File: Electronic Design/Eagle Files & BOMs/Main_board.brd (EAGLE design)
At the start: 99.9 x 68 mm, 36 parts, among them IC1 ACS712ELC-5A, IC2 ATMEGA328-PU, Q1 IRF9540, Q2 IRF9540, X1 16MHz

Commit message: adding header for additional DIO pins
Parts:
- added JP1: (no value), pinhead:1X05
- moved R5 8.54 mm to (79.1, 64.6), turned to 180 degrees
- moved S2 4.76 mm to (91.0, 63.8), turned to 180 degrees
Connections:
- new net N$20: IC2.14, JP1.5
- new net N$21: IC2.13, JP1.4
- new net N$22: IC2.12, JP1.3
- new net N$25: IC2.11, JP1.2
- net +5V: now also S2.2; no longer S2.1
- net GND: now also JP1.1
- net N$8: now also S2.4; no longer S2.3
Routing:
- net N$22: track 0.00 -> 14.9 mm
- net N$20: track 0.00 -> 14.9 mm
- net N$21: track 0.00 -> 14.9 mm
- net N$25: track 0.00 -> 14.8 mm
- net +5V: track 124.9 -> 111.1 mm
- net N$8: track 35.0 -> 34.0 mm
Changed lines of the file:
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@@
 <attribute name="VALUE" x="69.206034375" y="0.859565625" size="1.27" layer="27"/>
 </element>
-<element name="S2" library="switch-omron" package="B3F-10XX" value="" x="93.486315625" y="59.761790625" rot="R270">
-<attribute name="MPN" value="B3F-1000" x="93.486315625" y="59.761790625" size="1.778" layer="27" rot="R270" display="off"/>
-<attribute name="OC_FARNELL" value="176432" x="93.486315625" y="59.761790625" size="1.778" layer="27" rot="R270" display="off"/>
-<attribute name="OC_NEWARK" value="36M3542" x="93.486315625" y="59.761790625" size="1.778" layer="27" rot="R270" display="off"/>
-<attribute name="MF" value="" x="93.486315625" y="59.761790625" size="1.778" layer="27" rot="R270" display="off"/>
+<element name="S2" library="switch-omron" package="B3F-10XX" value="" x="91.021790625" y="63.833684375" rot="R180">
+<attribute name="MPN" value="B3F-1000" x="91.021790625" y="63.833684375" size="1.778" layer="27" rot="R180" display="off"/>
+<attribute name="OC_FARNELL" value="176432" x="91.021790625" y="63.833684375" size="1.778" layer="27" rot="R180" display="off"/>
+<attribute name="OC_NEWARK" value="36M3542" x="91.021790625" y="63.833684375" size="1.778" layer="27" rot="R180" display="off"/>
+<attribute name="MF" value="" x="91.021790625" y="63.833684375" size="1.778" layer="27" rot="R180" display="off"/>
 </element>
-<element name="R5" library="resistor" package="R1206" value="10k" x="87.245540625" y="62.122259375" rot="R90"/>
+<element name="R5" library="resistor" package="R1206" value="10k" x="79.077740625" y="64.605540625" rot="R180"/>
 <element name="POT1" library="resistor" package="RTRIM3296W" value="500k" x="63.175203125" y="54.911571875"/>
 <element name="D1" library="diode" package="DO35Z10" value="5.1V" x="70.7402" y="23.7643125" rot="R270"/>
@@
 </element>
 <element name="R6" library="varistor" package="S14K17" value="S14K75" x="15.67" y="51.73" rot="R270"/>
+<element name="JP1" library="pinhead" package="1X05" value="" x="97.05" y="53.75" smashed="yes" rot="R90">
+<attribute name="NAME" x="94.4312" y="54.2438" size="1.27" layer="25" ratio="10" rot="R90"/>
+<attribute name="VALUE" x="100.225" y="48.67" size="1.27" layer="27" rot="R90"/>
+</element>
 </elements>
 <signals>
@@
 <via x="89.61569375" y="42.3402" extent="1-16" drill="0.6" shape="square"/>
 <via x="89.41569375" y="39.5402" extent="1-16" drill="0.6" shape="square"/>
-<via x="94.41569375" y="49.1402" extent="1-16" drill="0.6" shape="square"/>
-<via x="85.81569375" y="54.5402" extent="1-16" drill="0.6" shape="square"/>
-<via x="87.81569375" y="54.1402" extent="1-16" drill="0.6" shape="square"/>
-<via x="92.61569375" y="54.5402" extent="1-16" drill="0.6" shape="square"/>
+<via x="93.97569375" y="47.0202" extent="1-16" drill="0.6" shape="square"/>
+<via x="59.33569375" y="57.8102" extent="1-16" drill="0.6" shape="square"/>
+<via x="49.50569375" y="60.0602" extent="1-16" drill="0.6" shape="square"/>
+<via x="96.14569375" y="31.6502" extent="1-16" drill="0.6" shape="square"/>
 <via x="87.81569375" y="44.3402" extent="1-16" drill="0.6" shape="square"/>
-<via x="94.324609375" y="52.94186875" extent="1-16" drill="0.6" shape="square"/>
+<via x="94.324609375" y="49.50186875" extent="1-16" drill="0.6" shape="square"/>
 <via x="92.8973" y="41.040346875" extent="1-16" drill="0.6" shape="square"/>
 <via x="75.41569375" y="63.5402" extent="1-16" drill="0.6" shape="square"/>
@@
 <vertex x="100.32" y="68.47"/>
 </polygon>
+<contactref element="JP1" pad="1"/>
 </signal>
 <signal name="M1S">
@@
 <wire x1="76.64795625" y1="47.329528125" x2="75.3559375" y2="47.329528125" width="0.6096" layer="1"/>
 <wire x1="75.3559375" y1="47.329528125" x2="75.1825375" y2="47.502928125" width="0.6096" layer="1"/>
-<contactref element="S2" pad="1"/>
 <wire x1="82.8025375" y1="42.422928125" x2="86.31648125" y2="42.422928125" width="0.6096" layer="1"/>
 <wire x1="86.31648125" y1="42.422928125" x2="86.71648125" y2="42.16599375" width="0.6096" layer="1"/>
@@
 <wire x1="75.1825375" y1="44.962928125" x2="69.234984375" y2="44.962928125" width="0.6096" layer="1"/>
 <wire x1="69.234984375" y1="44.962928125" x2="68.5950375" y2="45.00298125" width="0.6096" layer="1"/>
-<wire x1="95.746915625" y1="63.012990625" x2="95.746915625" y2="64.233084375" width="0.6096" layer="16"/>
-<wire x1="95.746915625" y1="64.233084375" x2="94.42" y2="65.56" width="0.6096" layer="16"/>
-<wire x1="94.42" y1="65.56" x2="79.22" y2="65.56" width="0.6096" layer="16"/>
-<wire x1="79.22" y1="65.56" x2="78.22" y2="64.56" width="0.6096" layer="16"/>
-<wire x1="78.22" y1="64.56" x2="78.22" y2="49.129528125" width="0.6096" layer="16"/>
-<wire x1="78.22" y1="49.129528125" x2="76.42" y2="47.329528125" width="0.6096" layer="16"/>
-<wire x1="76.42" y1="47.329528125" x2="75.3559375" y2="47.329528125" width="0.6096" layer="16"/>
-<wire x1="75.3559375" y1="47.329528125" x2="75.1825375" y2="47.502928125" width="0.6096" layer="16"/>
 <wire x1="68.5950375" y1="45.00298125" x2="67.23298125" y2="45.00298125" width="0.6096" layer="1"/>
 <wire x1="67.23298125" y1="45.00298125" x2="66.04" y2="43.81" width="0.6096" layer="1"/>
@@
 <wire x1="85.68" y1="13.68" x2="87.735384375" y2="13.68" width="0.6096" layer="1"/>
 <wire x1="87.735384375" y1="13.68" x2="87.81119375" y2="13.604190625" width="0.6096" layer="1"/>
+<contactref element="S2" pad="2"/>
+<wire x1="87.770590625" y1="61.573084375" x2="79.543084375" y2="61.573084375" width="0.6096" layer="16"/>
+<wire x1="79.543084375" y1="61.573084375" x2="78.61" y2="60.64" width="0.6096" layer="16"/>
+<wire x1="78.61" y1="60.64" x2="78.61" y2="48.94" width="0.6096" layer="16"/>
+<wire x1="78.61" y1="48.94" x2="77.28" y2="47.61" width="0.6096" layer="16"/>
+<wire x1="77.28" y1="47.61" x2="75.289609375" y2="47.61" width="0.6096" layer="16"/>
+<wire x1="75.289609375" y1="47.61" x2="75.1825375" y2="47.502928125" width="0.6096" layer="16"/>
 </signal>
 <signal name="N$15">
@@
 <signal name="N$8">
 <contactref element="IC2" pad="19"/>
-<contactref element="S2" pad="3"/>
 <contactref element="R5" pad="2"/>
 <contactref element="LED_CONTROL_OUT" pad="5"/>
-<wire x1="75.1825375" y1="50.042928125" x2="77.302928125" y2="50.042928125" width="0.6096" layer="1"/>
-<wire x1="77.302928125" y1="50.042928125" x2="78.82" y2="51.56" width="0.6096" layer="1"/>
-<wire x1="78.82" y1="51.56" x2="78.82" y2="62.76" width="0.6096" layer="1"/>
-<wire x1="78.82" y1="62.76" x2="79.62" y2="63.56" width="0.6096" layer="1"/>
-<wire x1="79.62" y1="63.56" x2="84.0298" y2="63.56" width="0.6096" layer="1"/>
-<wire x1="84.0298" y1="63.56" x2="87.245540625" y2="63.544259375" width="0.6096" layer="1"/>
-<wire x1="87.245540625" y1="63.544259375" x2="90.756984375" y2="63.544259375" width="0.6096" layer="1"/>
-<wire x1="90.756984375" y1="63.544259375" x2="91.225715625" y2="63.012990625" width="0.6096" layer="1"/>
 <wire x1="75.1825375" y1="50.042928125" x2="68.635090625" y2="50.042928125" width="0.6096" layer="1"/>
 <wire x1="68.635090625" y1="50.042928125" x2="68.5950375" y2="50.08298125" width="0.6096" layer="1"/>
+<contactref element="S2" pad="4"/>
+<wire x1="87.770590625" y1="66.094284375" x2="79.144484375" y2="66.094284375" width="0.6096" layer="1"/>
+<wire x1="79.144484375" y1="66.094284375" x2="77.655740625" y2="64.605540625" width="0.6096" layer="1"/>
+<wire x1="77.655740625" y1="64.605540625" x2="77.655740625" y2="50.705740625" width="0.6096" layer="1"/>
+<wire x1="77.655740625" y1="50.705740625" x2="76.92" y2="49.97" width="0.6096" layer="1"/>
+<wire x1="76.92" y1="49.97" x2="75.255465625" y2="49.97" width="0.6096" layer="1"/>
+<wire x1="75.255465625" y1="49.97" x2="75.1825375" y2="50.042928125" width="0.6096" layer="1"/>
 </signal>
 <signal name="N$4">
@@
 <wire x1="68.635090625" y1="39.882928125" x2="68.5950375" y2="39.92298125" width="0.6096" layer="1"/>
 </signal>
+<signal name="N$20">
+<contactref element="IC2" pad="14"/>
+<contactref element="JP1" pad="5"/>
+<wire x1="82.8025375" y1="60.202928125" x2="84.897071875" y2="60.202928125" width="0.6096" layer="1"/>
+<wire x1="84.897071875" y1="60.202928125" x2="86.35" y2="58.75" width="0.6096" layer="1"/>
+<wire x1="86.35" y1="58.75" x2="96.97" y2="58.75" width="0.6096" layer="1"/>
+<wire x1="96.97" y1="58.75" x2="97.05" y2="58.83" width="0.6096" layer="1"/>
+</signal>
+<signal name="N$21">
+<contactref element="IC2" pad="13"/>
+<contactref element="JP1" pad="4"/>
+<wire x1="82.8025375" y1="57.662928125" x2="93.187071875" y2="57.662928125" width="0.6096" layer="1"/>
+<wire x1="93.187071875" y1="57.662928125" x2="94.62" y2="56.23" width="0.6096" layer="1"/>
+<wire x1="94.62" y1="56.23" x2="96.99" y2="56.23" width="0.6096" layer="1"/>
+<wire x1="96.99" y1="56.23" x2="97.05" y2="56.29" width="0.6096" layer="1"/>
+</signal>
+<signal name="N$22">
+<contactref element="IC2" pad="12"/>
+<contactref element="JP1" pad="3"/>
+<wire x1="82.8025375" y1="55.122928125" x2="93.647071875" y2="55.122928125" width="0.6096" layer="1"/>
+<wire x1="93.647071875" y1="55.122928125" x2="95.11" y2="53.66" width="0.6096" layer="1"/>
+<wire x1="95.11" y1="53.66" x2="96.96" y2="53.66" width="0.6096" layer="1"/>
+<wire x1="96.96" y1="53.66" x2="97.05" y2="53.75" width="0.6096" layer="1"/>
+</signal>
+<signal name="N$25">
+<contactref element="IC2" pad="11"/>
+<contactref element="JP1" pad="2"/>
+<wire x1="82.8025375" y1="52.582928125" x2="93.577071875" y2="52.582928125" width="0.6096" layer="16"/>
+<wire x1="93.577071875" y1="52.582928125" x2="94.98" y2="51.18" width="0.6096" layer="16"/>
+<wire x1="94.98" y1="51.18" x2="97.02" y2="51.18" width="0.6096" layer="16"/>
+<wire x1="97.02" y1="51.18" x2="97.05" y2="51.21" width="0.6096" layer="16"/>
+</signal>
 </signals>

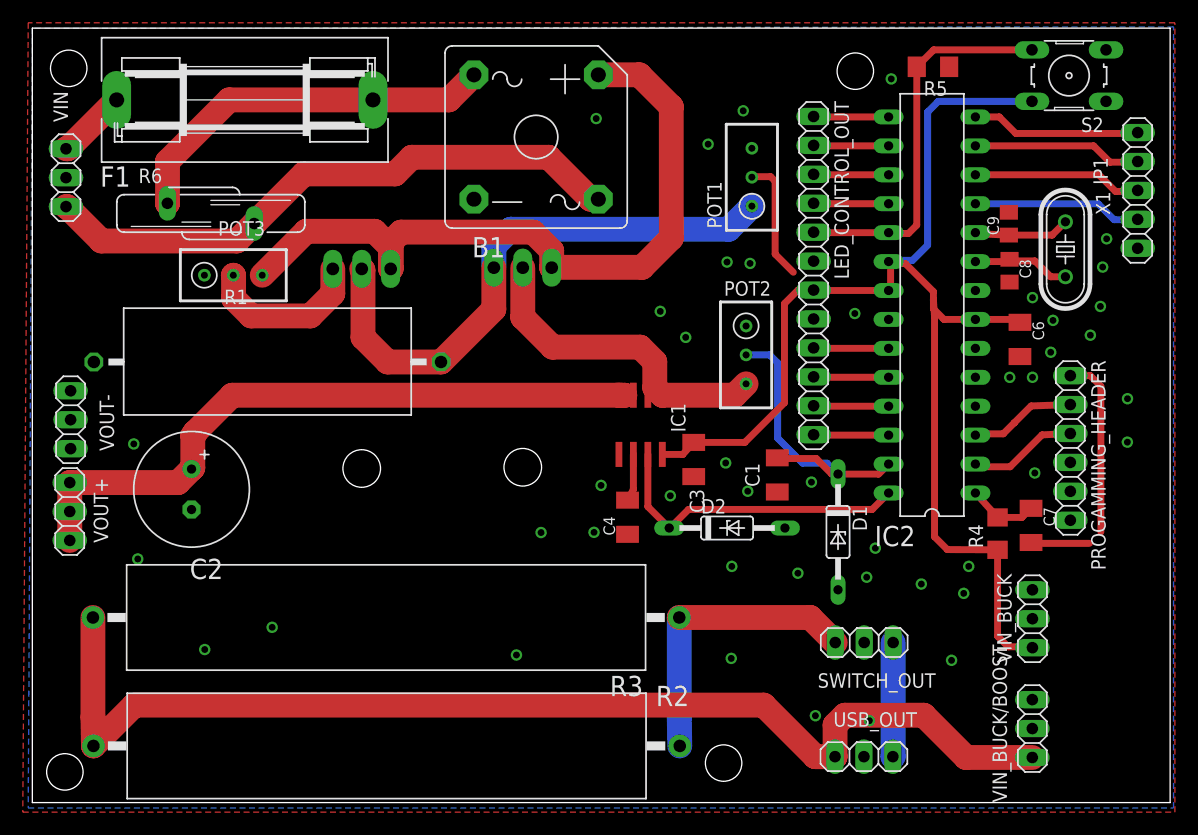
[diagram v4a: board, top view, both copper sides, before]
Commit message: fixing minor drc errors and repostionings monting holes
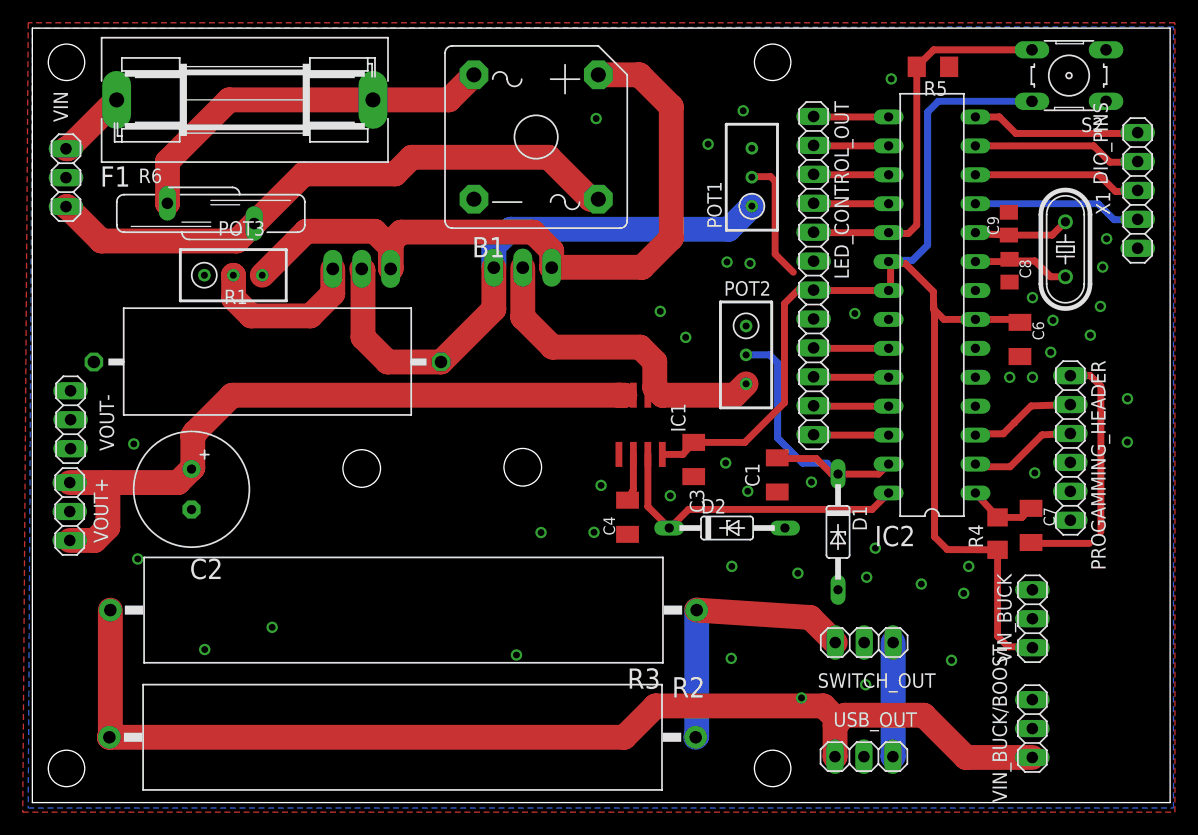
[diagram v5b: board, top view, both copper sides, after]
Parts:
- moved R3 1.66 mm to (32.6, 16.9)
- moved R2 1.59 mm to (32.5, 5.74)
- renumbered JP1 to DIO_PINS
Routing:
- net N$23: track 101.7 -> 98.9 mm
- net M1S: track 59.5 -> 62.1 mm
- net N$24: track 25.9 -> 24.3 mm
